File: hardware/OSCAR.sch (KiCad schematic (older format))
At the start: 24 parts

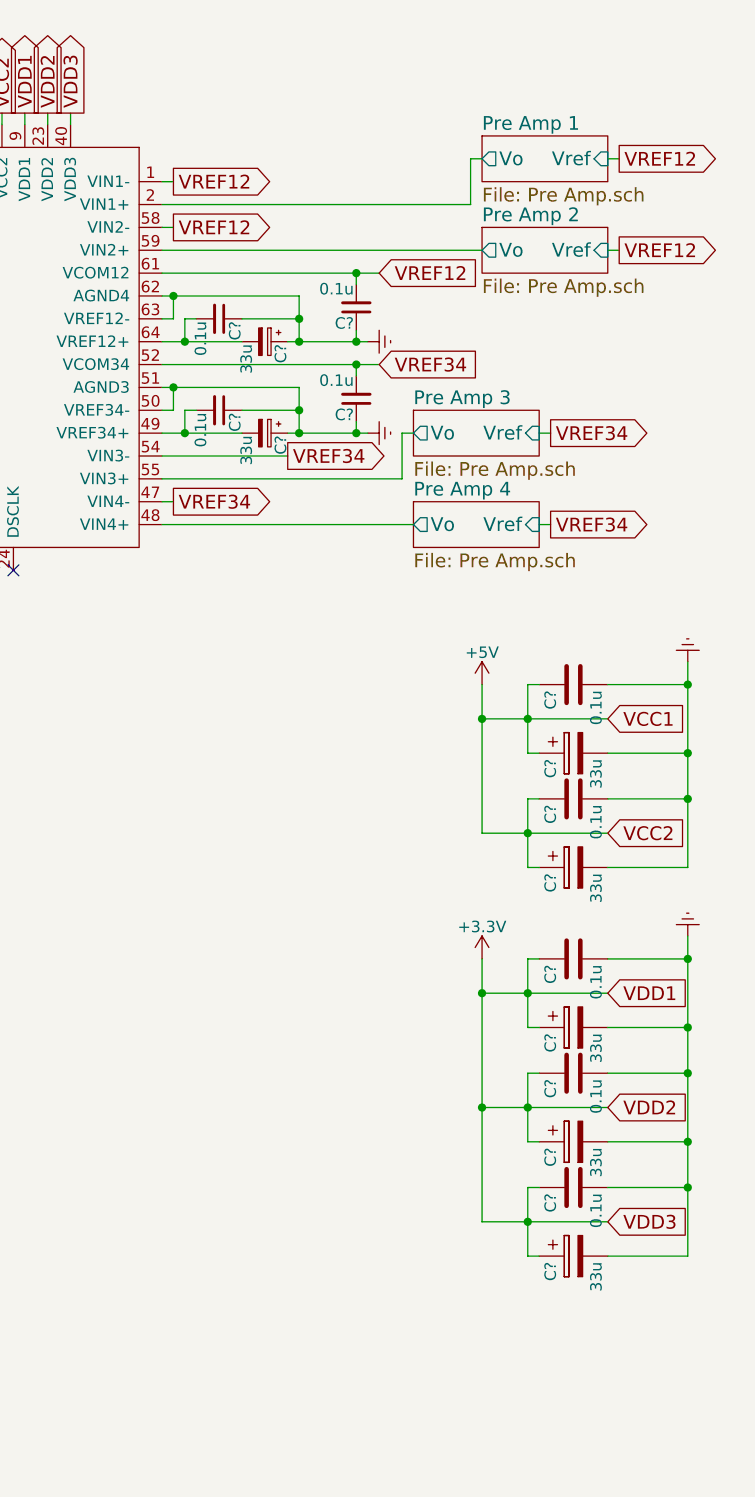
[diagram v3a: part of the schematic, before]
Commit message: Added voltage buffer to Vref
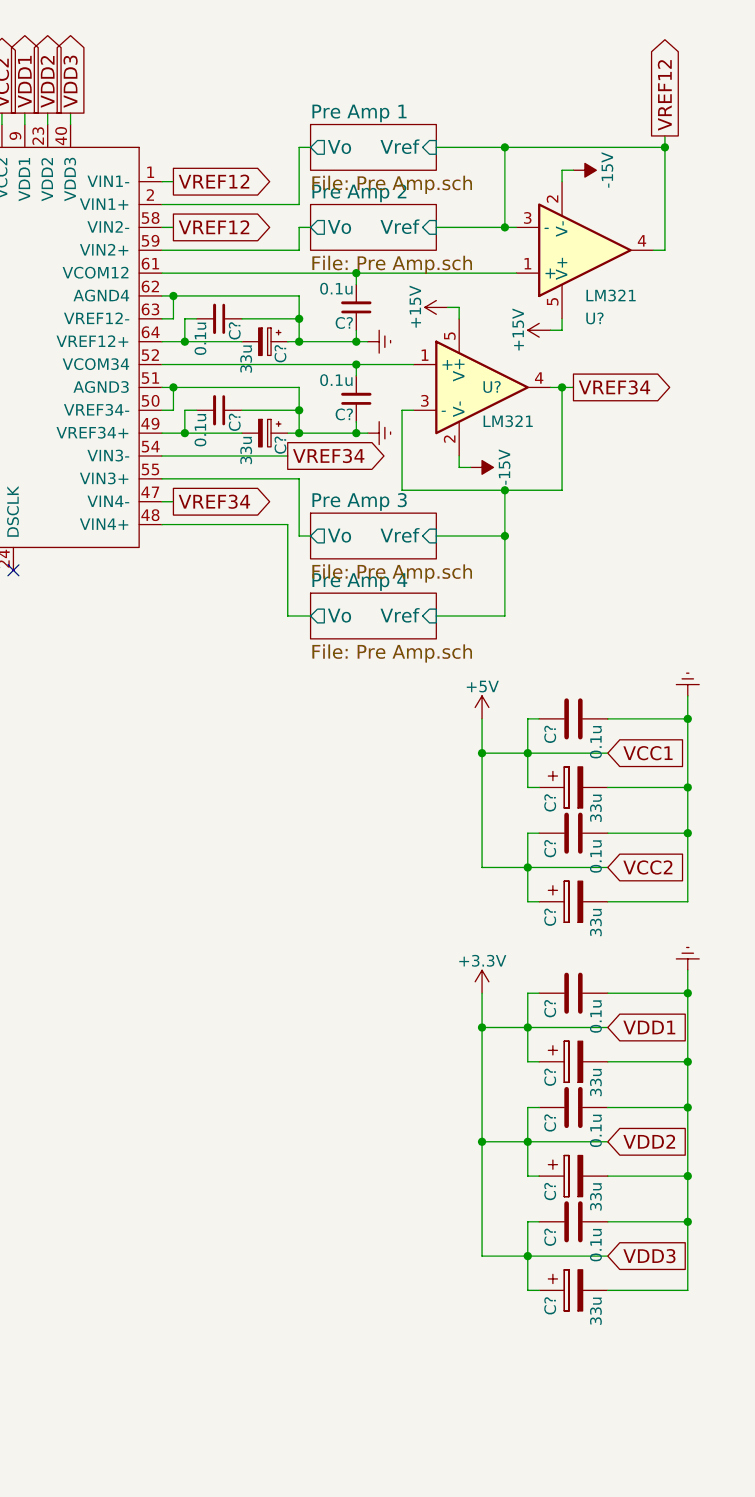
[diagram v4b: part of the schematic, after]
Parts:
- added U? (x2): LM321, TO_SOT_Packages_SMD:SOT-23-5, symbol LM321
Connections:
- net VREF12: now also U?.3 (-), U?.4; no longer C?.2, U?.61 (VCOM12)
- net VREF34: now also U?.3 (-), U?.4; no longer C?.2, U?.52 (VCOM34)
- new net: C?.2, U?.1 (+), U?.52 (VCOM34)
- new net: C?.2, U?.1 (+), U?.61 (VCOM12)
- new net +15V: U?.5 (V+), U?.5 (V+)
- new net -15V: U?.2 (V-), U?.2 (V-)
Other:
- moved on the sheet: C?

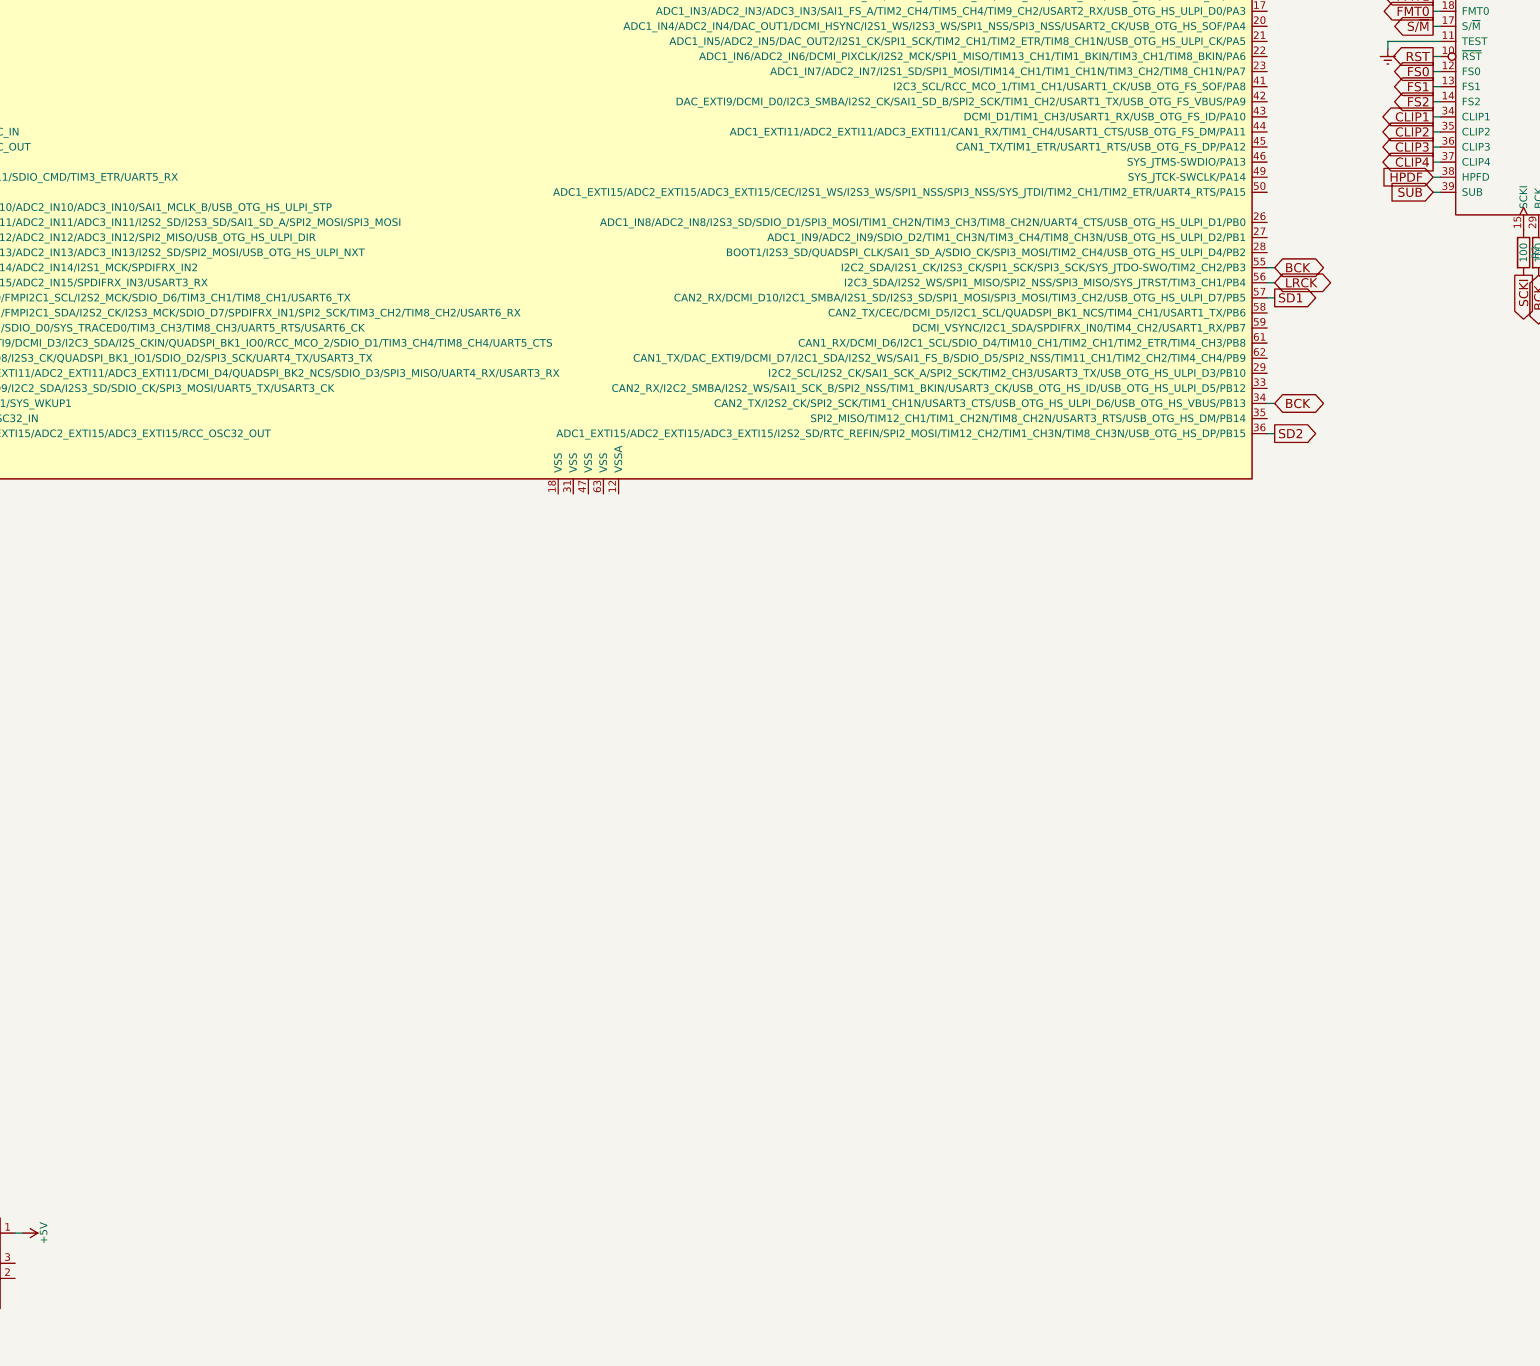
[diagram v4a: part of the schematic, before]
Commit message: Fixed direction on global labels and added 3.3v reg
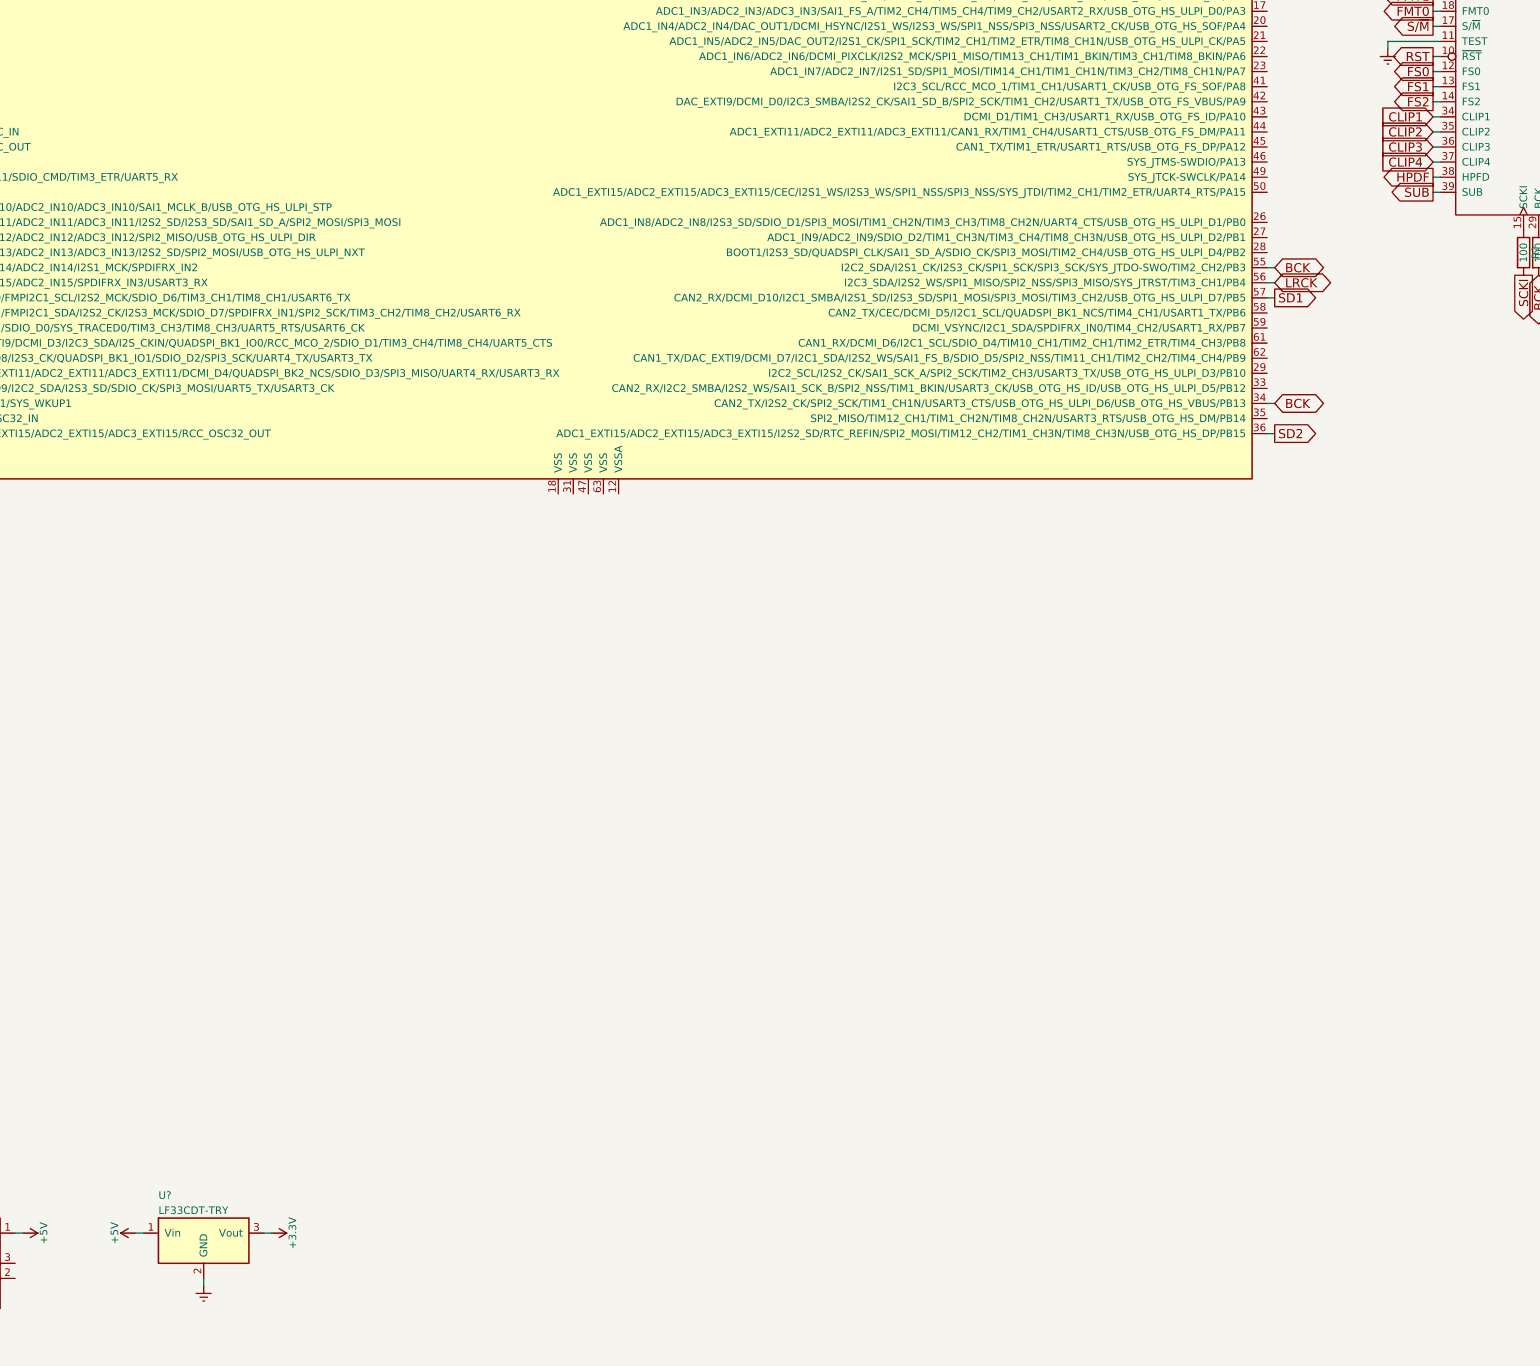
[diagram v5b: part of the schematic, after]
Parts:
- added U?: LF33CDT-TRY, TO_SOT_Packages_SMD:TO-252-2Lead, symbol LF33CDT-TRY
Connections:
- net +3V3: now also U?.3 (Vout)
- net +5V: now also U?.1 (Vin)
- net Earth: now also U?.2 (GND)
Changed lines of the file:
@@
 Text GLabel 11400 2000 0    60   Output ~ 0
 FS2
-Text GLabel 11400 2100 0    60   Output ~ 0
+Text GLabel 11400 2100 0    60   Input ~ 0
 CLIP1
-Text GLabel 11400 2200 0    60   Output ~ 0
+Text GLabel 11400 2200 0    60   Input ~ 0
 CLIP2
-Text GLabel 11400 2300 0    60   Output ~ 0
+Text GLabel 11400 2300 0    60   Input ~ 0
 CLIP3
-Text GLabel 11400 2400 0    60   Output ~ 0
+Text GLabel 11400 2400 0    60   Input ~ 0
 CLIP4
-Text GLabel 11400 2500 0    60   Input ~ 0
+Text GLabel 11400 2500 0    60   Output ~ 0
 HPDF
-Text GLabel 11400 2600 0    60   Input ~ 0
+Text GLabel 11400 2600 0    60   Output ~ 0
 SUB
 $Comp
@@
 $EndComp
 $Comp
-L +15V #PWR?
+L +15V #PWR011
 U 1 1 595CF51B
 P 14800 1700
-F 0 "#PWR?" H 14800 1550 50  0001 C CNN
+F 0 "#PWR011" H 14800 1550 50  0001 C CNN
 F 1 "+15V" H 14800 1840 50  0000 C CNN
 F 2 "" H 14800 1700 50  0001 C CNN
@@
 $EndComp
 $Comp
-L +15V #PWR?
+L +15V #PWR012
 U 1 1 595D0706
 P 15250 1800
-F 0 "#PWR?" H 15250 1650 50  0001 C CNN
+F 0 "#PWR012" H 15250 1650 50  0001 C CNN
 F 1 "+15V" H 15250 1940 50  0000 C CNN
 F 2 "" H 15250 1800 50  0001 C CNN
@@
 VREF34
 Connection ~ 15300 2050
+$Comp
+L LF33CDT-TRY U?
+U 1 1 595D853A
+P 3250 9600
+F 0 "U?" H 2950 9950 50  0000 L CNN
+F 1 "LF33CDT-TRY" H 2950 9850 50  0000 L CNN
+F 2 "TO_SOT_Packages_SMD:TO-252-2Lead" H 3250 9450 50  0001 L CNN
+F 3 "" H 3250 9750 50  0001 C CNN
+	1    3250 9600
+	1    0    0    -1
+$EndComp
+$Comp
+L +5V #PWR?
+U 1 1 595D8723
+P 2800 9500
+F 0 "#PWR?" H 2800 9350 50  0001 C CNN
+F 1 "+5V" H 2800 9640 50  0000 C CNN
+F 2 "" H 2800 9500 50  0001 C CNN
+F 3 "" H 2800 9500 50  0001 C CNN
+	1    2800 9500
+	0    -1   -1   0
+$EndComp
+$Comp
+L +3.3V #PWR?
+U 1 1 595D88C1
+P 3700 9500
+F 0 "#PWR?" H 3700 9350 50  0001 C CNN
+F 1 "+3.3V" H 3700 9640 50  0000 C CNN
+F 2 "" H 3700 9500 50  0001 C CNN
+F 3 "" H 3700 9500 50  0001 C CNN
+	1    3700 9500
+	0    1    1    0
+$EndComp
+$Comp
+L Earth #PWR?
+U 1 1 595D8AA0
+P 3250 9850
+F 0 "#PWR?" H 3250 9600 50  0001 C CNN
+F 1 "Earth" H 3250 9700 50  0001 C CNN
+F 2 "" H 3250 9850 50  0001 C CNN
+F 3 "" H 3250 9850 50  0001 C CNN
+	1    3250 9850
+	1    0    0    -1
+$EndComp
+Wire Wire Line
+	2800 9500 2850 9500
+Wire Wire Line
+	3250 9850 3250 9800
+Wire Wire Line
+	3700 9500 3650 9500
 $EndSCHEMATC

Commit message: Began stm32 power wiring
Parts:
- added C?: 2.2u, symbol C_Small
- added C? (x5): 100n, symbol C_Small
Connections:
- net +3V3: now also U?.13 (VDDA), U?.19 (VDD), U?.32 (VDD), U?.48 (VDD), U?.64 (VDD), C?.2, C?.2, C?.2, C?.2, C?.2
- net Earth: now also U?.12 (VSSA), U?.18 (VSS), U?.31 (VSS), U?.47 (VSS), U?.63 (VSS), C?.1, C?.1, C?.1, C?.1, C?.1, C?.2
- net at U?.30 (VCAP_1): now also C?.1
- net DM: now reaches U?.44 (ADC1_EXTI11/ADC2_EXTI11/ADC3_EXTI11/CAN1_RX/TIM1_CH4/USART1_CTS/USB_OTG_FS_DM/PA11)
- net DM: now also J?.3 (D+)
- net DP: now reaches U?.45 (CAN1_TX/TIM1_ETR/USART1_RTS/USB_OTG_FS_DP/PA12)
- net DP: now also J?.2 (D-)
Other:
- note added: "3.3V Power Decoupling"
- note added: "3.3V Regulator"
- note added: "5V Power Decoupling"
- moved on the sheet: C?, U?

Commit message: Moved from global labels to busses
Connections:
- net DM: now also J?.2 (D-); no longer J?.3 (D+)
- net DP: now also J?.3 (D+); no longer J?.2 (D-)
- net HPDF renamed HPFD
- net VREF12 renamed Vref12
- net VREF34 renamed Vref34
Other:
- moved on the sheet: C?, J?, R?, U?

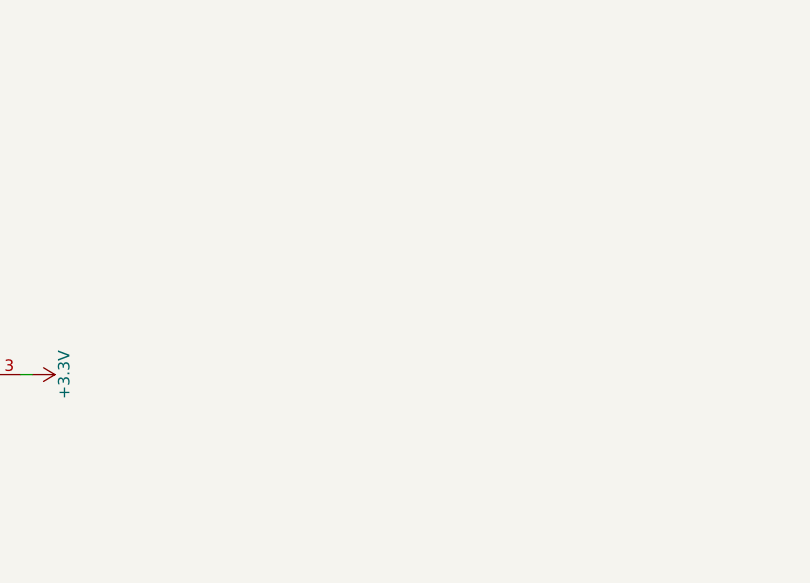
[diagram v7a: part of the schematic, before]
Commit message: Added +- 18V regulator
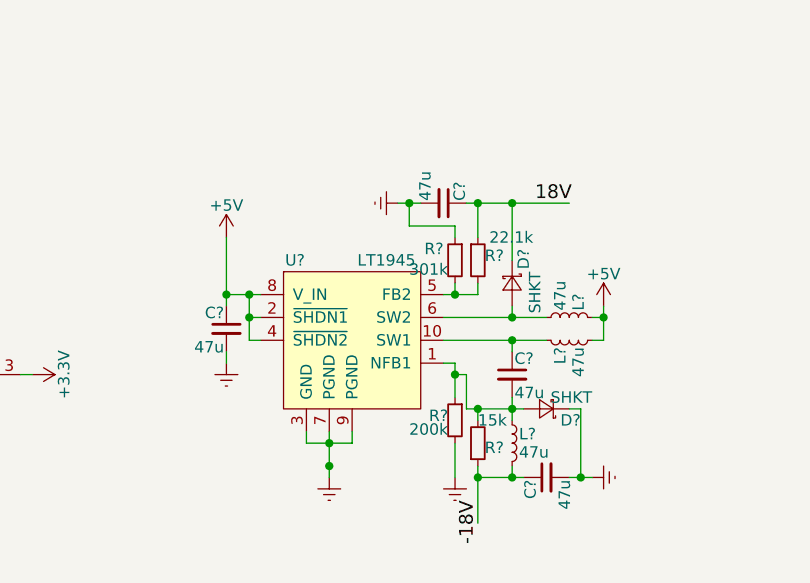
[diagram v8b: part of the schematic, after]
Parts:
- added C? (x4): 47u, symbol C_Small
- added D? (x2): SHKT, symbol D_Schottky_Small
- added L? (x3): 47u, symbol L_Small
- added R?: 15k, symbol R_Small
- added R?: 200k, symbol R_Small
- added R?: 22.1k, symbol R_Small
- added R?: 301k, symbol R_Small
- added U?: LT1945, symbol LT1945
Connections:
- net +5V: now also C?.1, L?.1, L?.2, U?.2 (~SHDN1), U?.4 (~SHDN2), U?.8 (V_IN)
- net Earth: now also C?.2, C?.2, C?.2, D?.1 (K), R?.1, R?.2, U?.3 (GND), U?.7 (PGND), U?.9 (PGND)
- new net: C?.2, D?.2 (A), L?.1, R?.1, R?.2, U?.1 (NFB1)
- new net: C?.1, L?.1, U?.10 (SW1)
- new net: R?.2, R?.2, U?.5 (FB2)
- new net: D?.2 (A), L?.2, U?.6 (SW2)
- new net -18V: C?.1, L?.2, R?.1
- new net 18V: C?.1, D?.1 (K), R?.1
